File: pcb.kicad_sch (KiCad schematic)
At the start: 32 parts, among them J2 USB_C_Receptacle_USB2.0, SW1 SW_Push, U1 ADXL375, U2 ESP32-S3-MINI-1, U3 AMS1117-3.3, U4 MCP73831-2-OT, U5 W25Q128JVS

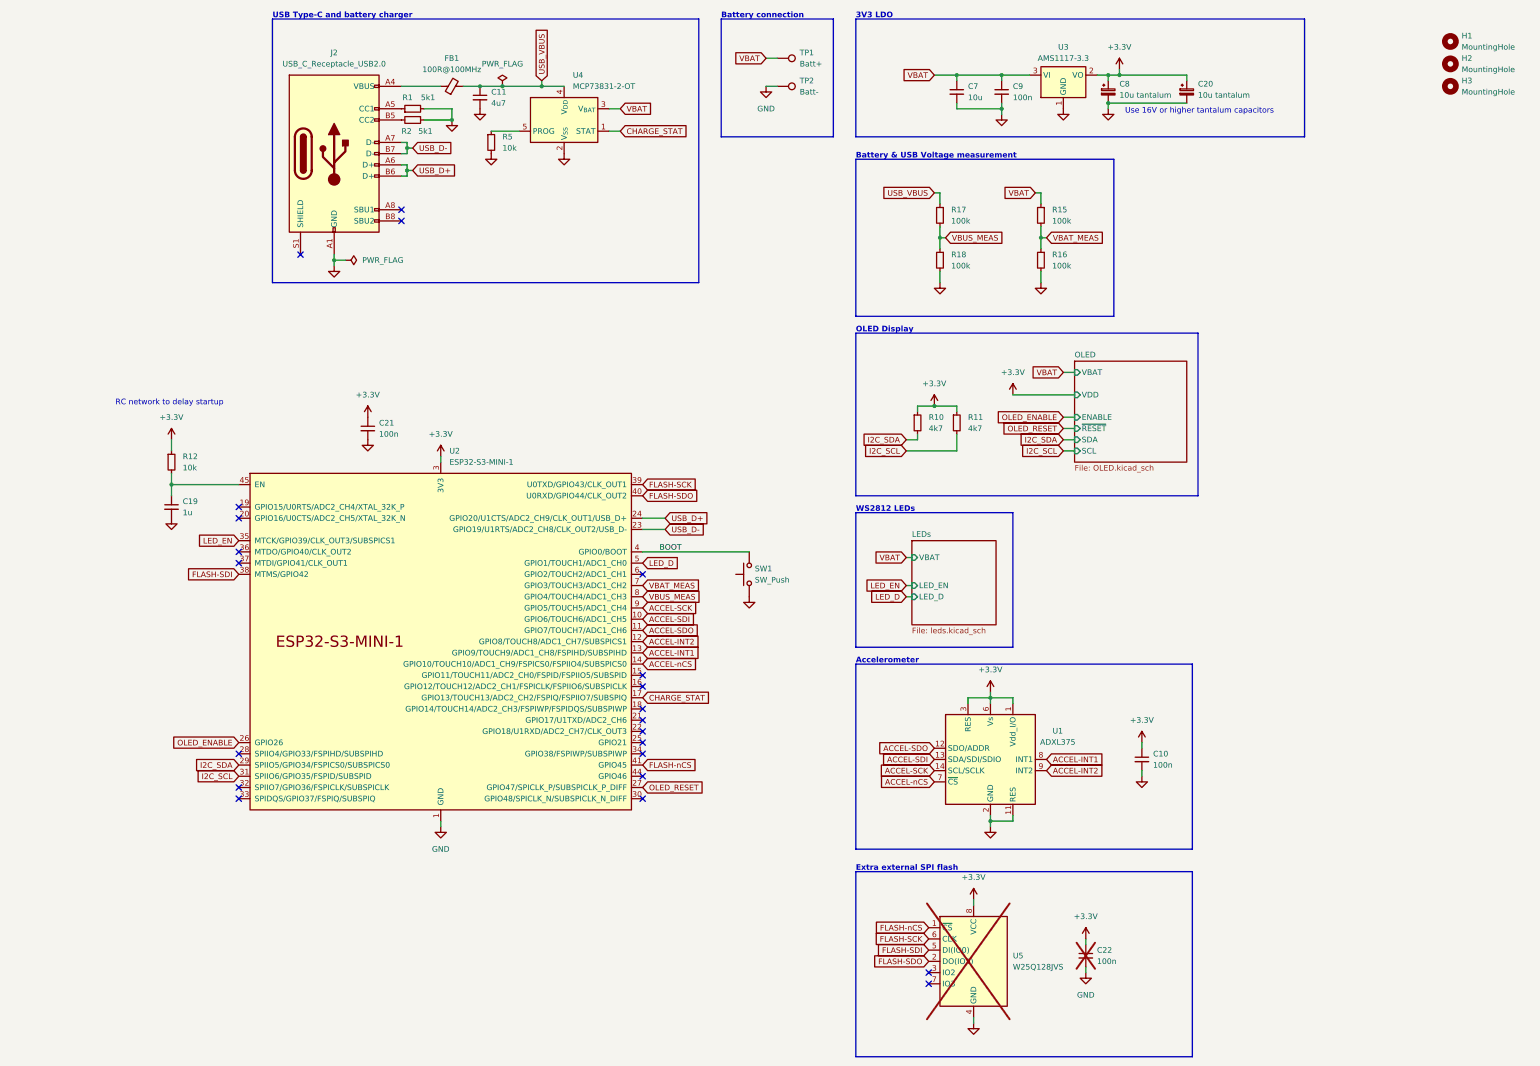
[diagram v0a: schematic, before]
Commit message: Use bare ESP32 chip instead of module (#1)
* fixed library issues

* add submodules to CI/CD

* fix yaml syntax

* added part numbers

* Bare ESP layout

* fix erc/drc

* fix overlap

* added part numbers

* fixed layout
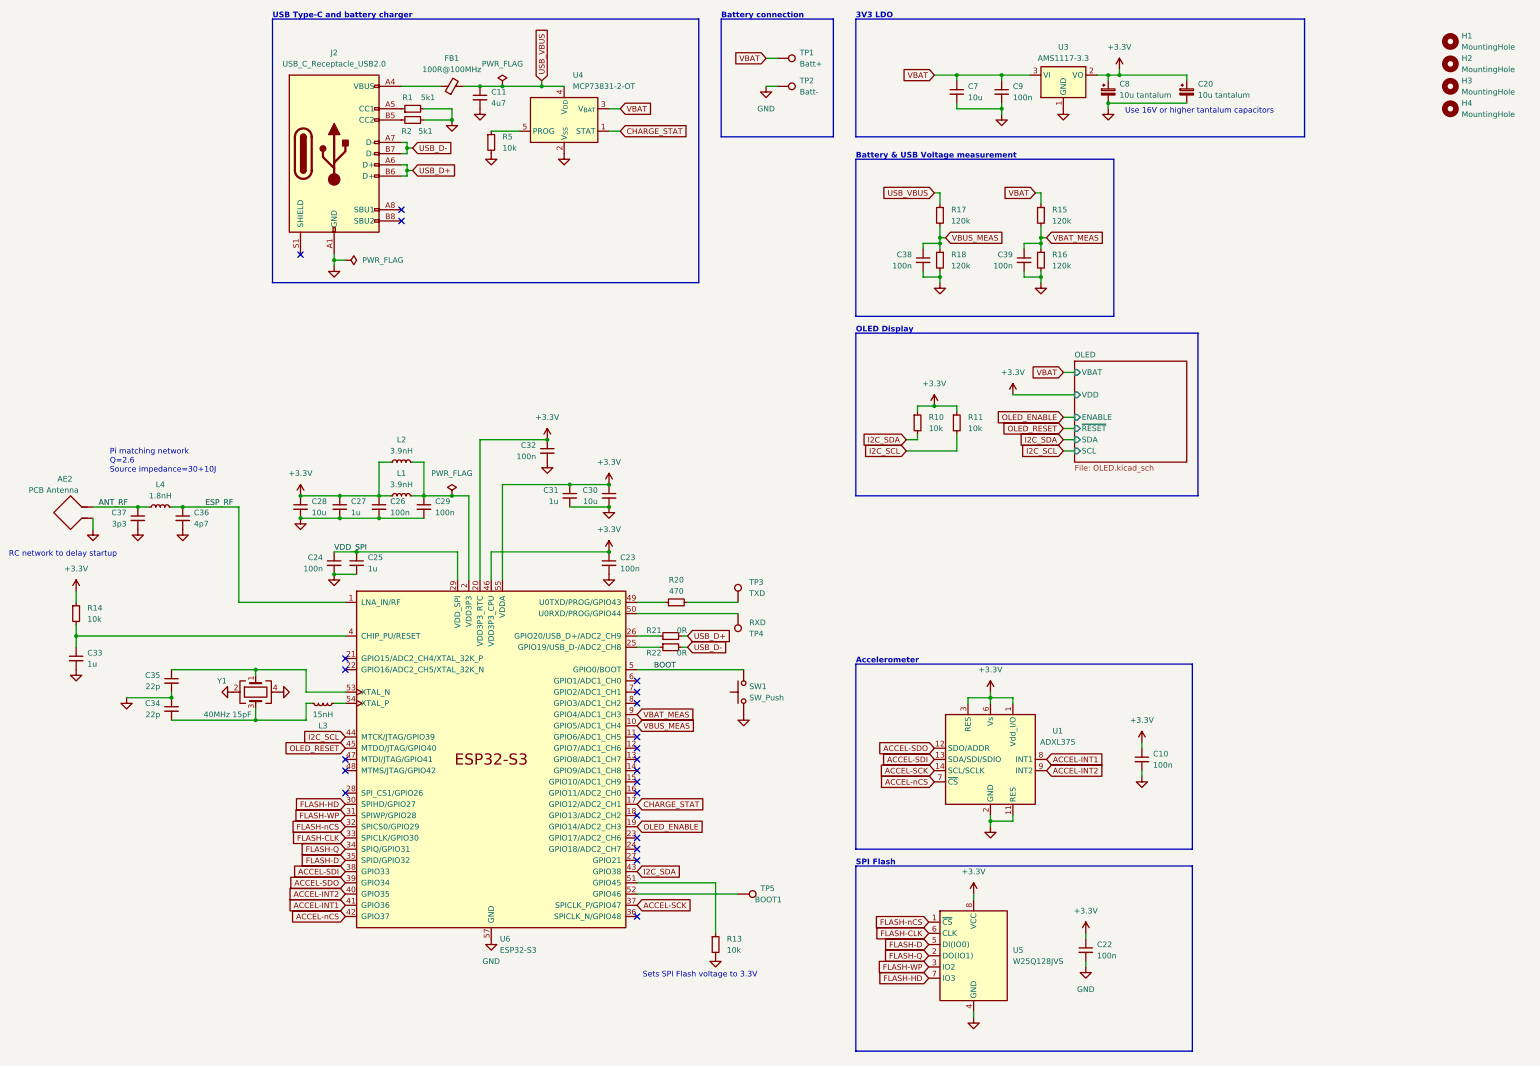
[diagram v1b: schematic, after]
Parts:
- removed C19: 1u, Capacitor_SMD:C_0402_1005Metric, symbol Device:C_Small
- removed C21: 100n, Capacitor_SMD:C_0402_1005Metric, symbol Device:C_Small
- removed R12: 10k, Capacitor_SMD:C_0402_1005Metric, symbol Device:R_Small
- removed U2: ESP32-S3-MINI-1, PCM_Espressif:ESP32-S2-MINI-1, symbol PCM_Espressif:ESP32-S3-MINI-1
- added AE2: PCB Antenna, RF_Antenna:Texas_SWRA117D_2.4GHz_Left, symbol Device:Antenna_Loop
- added C23, C24, C26, C29, C32, C38, C39: 100n, Capacitor_SMD:C_0402_1005Metric, symbol Device:C_Small
- added C25, C27, C31, C33: 1u, Capacitor_SMD:C_0402_1005Metric, symbol Device:C_Small
- added C28, C30: 10u, Capacitor_SMD:C_0402_1005Metric, symbol Device:C_Small
- added C34, C35: 22p, Capacitor_SMD:C_0402_1005Metric, symbol Device:C_Small
- added C36: 4p7, Capacitor_SMD:C_0402_1005Metric, symbol Device:C_Small
- added C37: 3p3, Capacitor_SMD:C_0402_1005Metric, symbol Device:C_Small
- added H4: MountingHole, MountingHole:MountingHole_2.2mm_M2, symbol Mechanical:MountingHole
- added L1, L2: 3.9nH, Inductor_SMD:L_0402_1005Metric, symbol Device:L_Small
- added L3: 15nH, Inductor_SMD:L_0402_1005Metric, symbol Device:L_Small
- added L4: 1.8nH, Inductor_SMD:L_0402_1005Metric, symbol Device:L_Small
- added R13, R14: 10k, Resistor_SMD:R_0402_1005Metric, symbol Device:R_Small
- added R20: 470, Resistor_SMD:R_0402_1005Metric, symbol Device:R_Small
- added R21, R22: 0R, Resistor_SMD:R_0402_1005Metric, symbol Device:R_Small
- added TP3: TXD, TestPoint:TestPoint_Pad_D1.0mm, symbol Connector:TestPoint
- added TP4: RXD, TestPoint:TestPoint_Pad_D1.0mm, symbol Connector:TestPoint
- added TP5: BOOT1, TestPoint:TestPoint_Pad_D1.0mm, symbol Connector:TestPoint
- added U6: ESP32-S3, Package_DFN_QFN:QFN-56-1EP_7x7mm_P0.4mm_EP5.6x5.6mm, symbol Espressif:ESP32-S3
- added Y1: 40MHz 15pF, Crystal:Crystal_SMD_3225-4Pin_3.2x2.5mm, symbol Device:Crystal_GND24
- C10, C9: LCSC (none) -> C1525
- C11: LCSC (none) -> C23733
- C20, C8: LCSC (none) -> C7171
- C22: LCSC (none) -> C1525; now fitted
- C7: LCSC (none) -> C15525
- R10, R11: value 4k7 -> 10k; footprint Capacitor_SMD:C_0402_1005Metric -> Resistor_SMD:R_0402_1005Metric; LCSC (none) -> C25086
- R15, R16, R17, R18: value 100k -> 120k; footprint Capacitor_SMD:C_0402_1005Metric -> Resistor_SMD:R_0402_1005Metric; LCSC (none) -> C25750
- R5: footprint Capacitor_SMD:C_0402_1005Metric -> Resistor_SMD:R_0402_1005Metric; LCSC (none) -> C25086
- U1: LCSC (none) -> C481898
- U3: LCSC (none) -> C6186
- U4: LCSC (none) -> C841234
- U5: LCSC (none) -> C97521; now fitted
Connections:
- net +3.3V: now also C23.1, C26.1, C27.1, C28.1, C30.1, C31.1, C32.1, L1.1, L2.1, R14.1, U6.20 (VDD3P3_RTC), U6.46 (VDD3P3_CPU), U6.55 (VDDA), U6.56 (VDDA)
- net ACCEL-INT1: now also U6.41 (GPIO36)
- net ACCEL-INT2: now also U6.40 (GPIO35)
- net ACCEL-SCK: now also U6.37 (SPICLK_P/GPIO47)
- net ACCEL-SDI: now also U6.38 (GPIO33)
- net ACCEL-SDO: now also U6.39 (GPIO34)
- net ACCEL-nCS: now also U6.42 (GPIO37)
- net BOOT: now also U6.5 (GPIO0/BOOT)
- net CHARGE_STAT: now also U6.17 (GPIO12/ADC2_CH1)
- net FLASH-nCS: now also U6.32 (SPICS0/GPIO29)
- net GND: now also AE2.2, C23.2, C24.2, C25.2, C26.2, C27.2, C28.2, C29.2, C30.2, C31.2, C32.2, C33.2, C34.1, C35.2, C36.2, C37.2, C38.2, C39.2, R13.2, U6.57 (GND), Y1.2, Y1.4
- net I2C_SCL: now also U6.44 (MTCK/JTAG/GPIO39)
- net I2C_SDA: now also U6.43 (GPIO38)
- net OLED_ENABLE: now also U6.19 (GPIO14/ADC2_CH3)
- net OLED_RESET: now also U6.45 (MTDO/JTAG/GPIO40)
- net USB_D+: now also R21.2
- net USB_D-: now also R22.2
- net VBAT_MEAS: now also C39.1, U6.9 (GPIO4/ADC1_CH3)
- net VBUS_MEAS: now also C38.1, U6.10 (GPIO5/ADC1_CH4)
- net FLASH-WP: now reaches U5.3 (IO2)
- net FLASH-WP: now also U6.31 (SPIWP/GPIO28)
- net FLASH-HD: now reaches U5.7 (IO3)
- net FLASH-HD: now also U6.30 (SPIHD/GPIO27)
- net FLASH-SCK renamed FLASH-CLK
- net FLASH-CLK: now also U6.33 (SPICLK/GPIO30)
- net FLASH-SDI renamed FLASH-D
- net FLASH-D: now also U6.35 (SPID/GPIO32)
- net FLASH-SDO renamed FLASH-Q
- net FLASH-Q: now also U6.34 (SPIQ/GPIO31)
- new net: C34.2, L3.1, Y1.3
- new net: L3.2, U6.54 (XTAL_P)
- new net: R20.1, U6.49 (U0TXD/PROG/GPIO43)
- new net: R20.2, TP3.1
- new net: C33.1, R14.2, U6.4 (CHIP_PU/RESET)
- new net: R22.1, U6.25 (GPIO19/USB_D-/ADC2_CH8)
- new net: R21.1, U6.26 (GPIO20/USB_D+/ADC2_CH9)
- new net: TP4.1, U6.50 (U0RXD/PROG/GPIO44)
- new net: R13.1, U6.51 (GPIO45)
- new net: C35.1, U6.53 (XTAL_N), Y1.1
- new net: TP5.1, U6.52 (GPIO46)
- new net ANT_RF: AE2.1, C37.1, L4.1
- new net ESP_RF: C36.1, L4.2, U6.1 (LNA_IN/RF)
- new net VDD3P3: C29.1, L1.2, L2.2, U6.2 (VDD3P3), U6.3 (VDD3P3)
- new net VDD_SPI: C24.1, C25.1, U6.29 (VDD_SPI)
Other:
- removed sheet LEDs
- note added: "Pi matching network Q=2.6 Source impedance=30+10J"
- note added: "SPI Flash"
- note added: "Sets SPI Flash voltage to 3.3V"
- note removed: "Extra external SPI flash"
- note removed: "WS2812 LEDs"
- moved on the sheet: SW1

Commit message: Incorporate feedback from cnlohr
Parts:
- added R1: 10k, Resistor_SMD:R_0402_1005Metric, symbol Device:R_Small
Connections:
- net +3.3V: now also R1.1
- net BOOT: now also R1.2
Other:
- moved on the sheet: SW1
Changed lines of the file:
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@@
   (junction (at 123.19 48.26) (diameter 0) (color 0 0 0 0)
   )
+  (junction (at 190.5 180.34) (diameter 0) (color 0 0 0 0)
+  )
   (junction (at 138.43 128.27) (diameter 0) (color 0 0 0 0)
   )
@@
     (stroke (width 0) (type default))
   )
-  (wire (pts (xy 158.75 180.34) (xy 182.88 180.34))
+  (wire (pts (xy 158.75 180.34) (xy 190.5 180.34))
     (stroke (width 0) (type default))
   )
@@
     )
   )
+  (symbol (lib_id "power:+3.3V") (at 190.5 175.26 0) (unit 1)
+    (in_bom yes) (on_board yes) (dnp no) (fields_autoplaced)
+    (property "Reference" "#PWR01" (at 190.5 179.07 0)
+      (effects (font (size 1.27 1.27)) hide)
+    )
+    (property "Value" "+3.3V" (at 190.5 170.18 0)
+      (effects (font (size 1.27 1.27)))
+    )
+    (property "Footprint" "" (at 190.5 175.26 0)
+      (effects (font (size 1.27 1.27)) hide)
+    )
+    (property "Datasheet" "" (at 190.5 175.26 0)
+      (effects (font (size 1.27 1.27)) hide)
+    )
+    (pin "1")
+    (instances
+      (project "pcb"
+        (path "/74bf6178-dca6-4427-901b-44badacb7eee"
+          (reference "#PWR01") (unit 1)
+        )
+      )
+    )
+  )
   (symbol (lib_id "power:+3.3V") (at 273.05 196.85 0) (unit 1)
     (in_bom yes) (on_board yes) (dnp no) (fields_autoplaced)
@@
     )
   )
-  (symbol (lib_id "Switch:SW_Push") (at 182.88 185.42 90) (unit 1)
+  (symbol (lib_id "Switch:SW_Push") (at 190.5 185.42 90) (unit 1)
     (in_bom yes) (on_board yes) (dnp no) (fields_autoplaced)
-    (property "Reference" "SW1" (at 184.15 184.1499 90)
+    (property "Reference" "SW1" (at 191.77 184.1499 90)
       (effects (font (size 1.27 1.27)) (justify right))
     )
-    (property "Value" "SW_Push" (at 184.15 186.6899 90)
+    (property "Value" "SW_Push" (at 191.77 186.6899 90)
       (effects (font (size 1.27 1.27)) (justify right))
     )
-    (property "Footprint" "Button_Switch_SMD:SW_Push_1P1T_NO_CK_KSC7xxJ" (at 177.8 185.42 0)
+    (property "Footprint" "Button_Switch_SMD:SW_Push_1P1T_NO_CK_KSC7xxJ" (at 185.42 185.42 0)
       (effects (font (size 1.27 1.27)) hide)
     )
-    (property "Datasheet" "~" (at 177.8 185.42 0)
+    (property "Datasheet" "~" (at 185.42 185.42 0)
       (effects (font (size 1.27 1.27)) hide)
     )
-    (property "LCSC" "C318884" (at 182.88 185.42 0)
+    (property "LCSC" "C318884" (at 190.5 185.42 0)
       (effects (font (size 1.27 1.27)) hide)
     )
@@
     )
   )
+  (symbol (lib_id "Device:R_Small") (at 190.5 177.8 0) (unit 1)
+    (in_bom yes) (on_board yes) (dnp no) (fields_autoplaced)
+    (property "Reference" "R1" (at 193.04 176.53 0)
+      (effects (font (size 1.27 1.27)) (justify left))
+    )
+    (property "Value" "10k" (at 193.04 179.07 0)
+      (effects (font (size 1.27 1.27)) (justify left))
+    )
+    (property "Footprint" "Resistor_SMD:R_0402_1005Metric" (at 190.5 177.8 0)
+      (effects (font (size 1.27 1.27)) hide)
+    )
+    (property "Datasheet" "~" (at 190.5 177.8 0)
+      (effects (font (size 1.27 1.27)) hide)
+    )
+    (property "LCSC" "C25086" (at 190.5 177.8 0)
+      (effects (font (size 1.27 1.27)) hide)
+    )
+    (pin "1")
+    (pin "2")
+    (instances
+      (project "pcb"
+        (path "/74bf6178-dca6-4427-901b-44badacb7eee"
+          (reference "R1") (unit 1)
+        )
+      )
+    )
+  )
   (symbol (lib_id "power:GND") (at 43.18 186.69 0) (mirror y) (unit 1)
     (in_bom yes) (on_board yes) (dnp no)
@@
     )
   )
-  (symbol (lib_id "power:GND") (at 182.88 190.5 0) (unit 1)
+  (symbol (lib_id "power:GND") (at 190.5 190.5 0) (unit 1)
     (in_bom yes) (on_board yes) (dnp no) (fields_autoplaced)
-    (property "Reference" "#PWR032" (at 182.88 196.85 0)
+    (property "Reference" "#PWR032" (at 190.5 196.85 0)
       (effects (font (size 1.27 1.27)) hide)
     )
-    (property "Value" "GND" (at 182.88 195.58 0)
+    (property "Value" "GND" (at 190.5 195.58 0)
       (effects (font (size 1.27 1.27)) hide)
     )
-    (property "Footprint" "" (at 182.88 190.5 0)
+    (property "Footprint" "" (at 190.5 190.5 0)
       (effects (font (size 1.27 1.27)) hide)
     )
-    (property "Datasheet" "" (at 182.88 190.5 0)
+    (property "Datasheet" "" (at 190.5 190.5 0)
       (effects (font (size 1.27 1.27)) hide)
     )
